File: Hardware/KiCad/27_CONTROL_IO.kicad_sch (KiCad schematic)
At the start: 0 parts

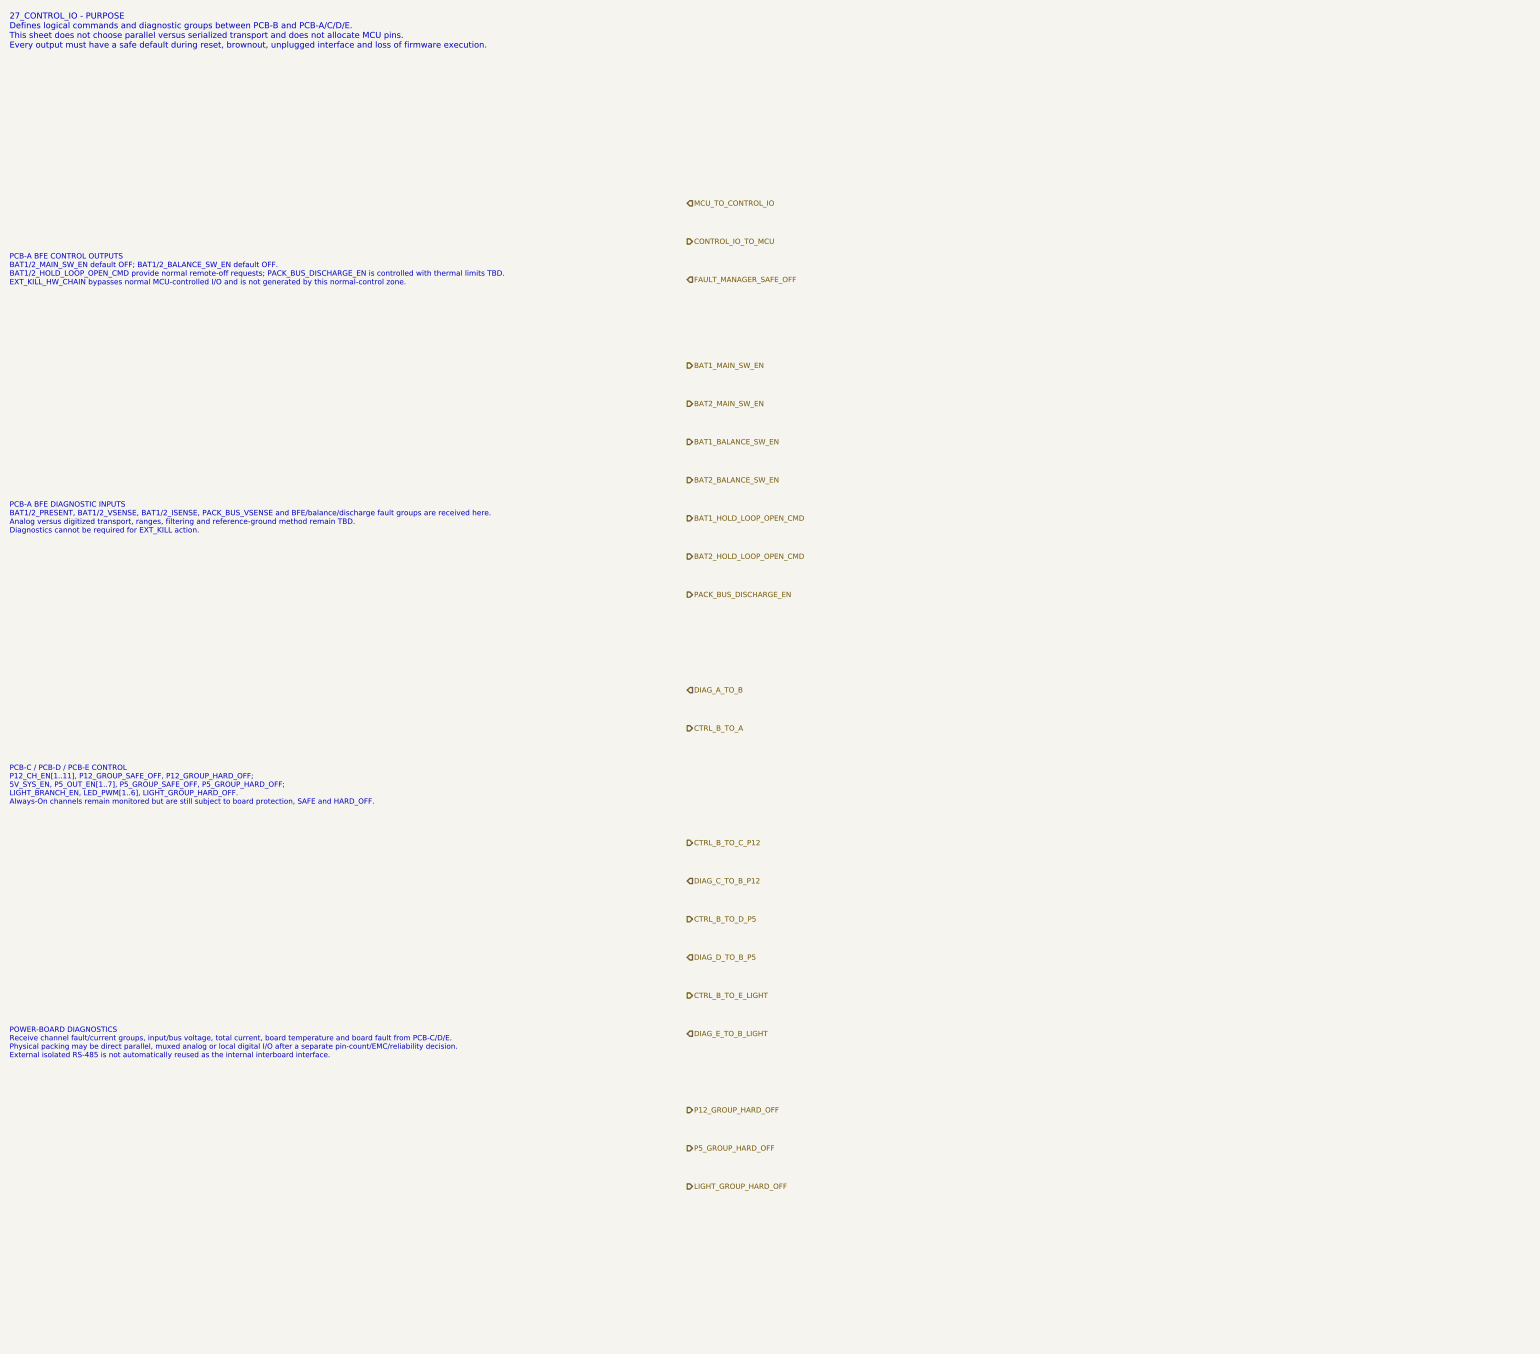
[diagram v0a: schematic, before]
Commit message: hardware: complete PCB-B control and diagnostic interfaces
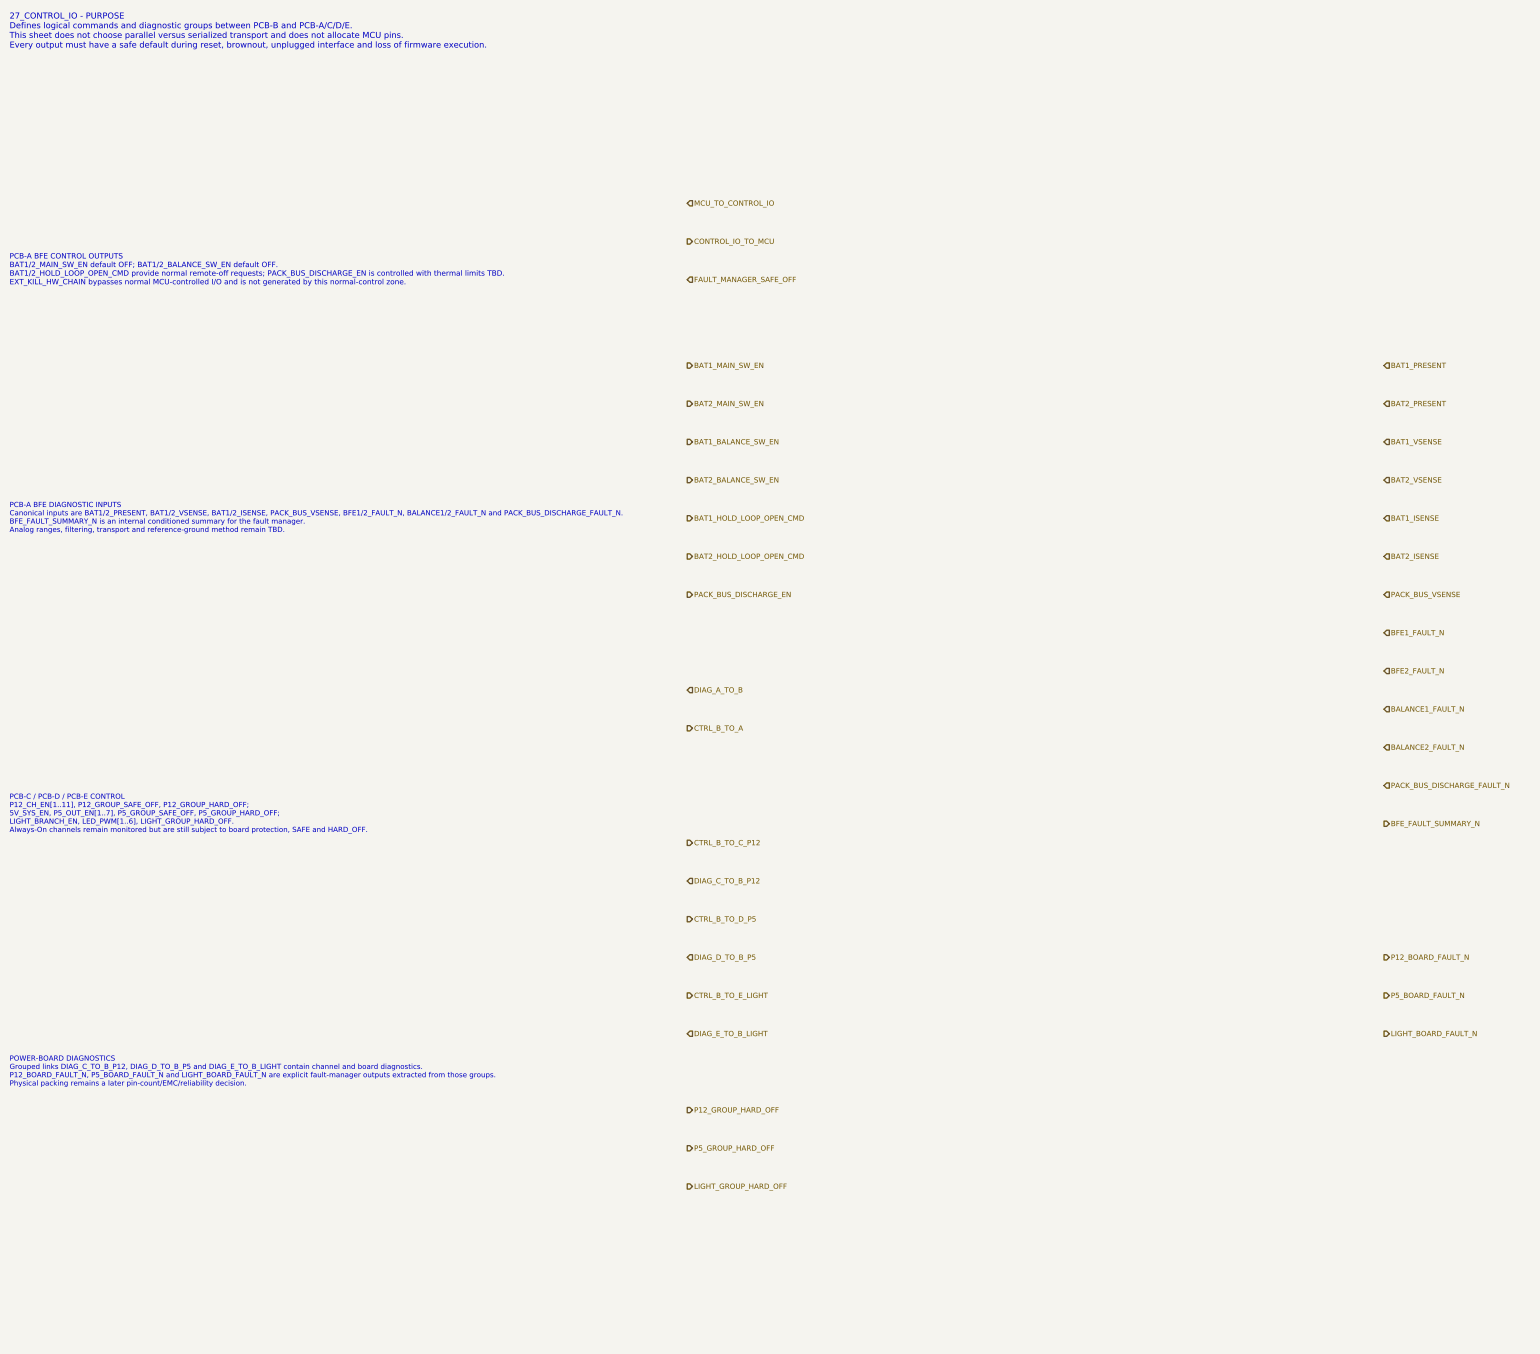
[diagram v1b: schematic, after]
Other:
- note added: "PCB-A BFE DIAGNOSTIC INPUTS Canonical inputs are BAT1/2_PRESENT, BAT1/2_VSENSE, BAT1/2_ISENSE, PACK_BUS_VSENSE, BFE1/2_FAULT_N, BALANCE1/2_FAULT_N and PACK_BUS_DISCHARGE_FAULT_N. BFE_FAULT_SUMMARY_N is an internal conditioned summary for the fault manager. Analog ranges, filtering, transport and reference-ground method remain TBD."
- note added: "POWER-BOARD DIAGNOSTICS Grouped links DIAG_C_TO_B_P12, DIAG_D_TO_B_P5 and DIAG_E_TO_B_LIGHT contain channel and board diagnostics. P12_BOARD_FAULT_N, P5_BOARD_FAULT_N and LIGHT_BOARD_FAULT_N are explicit fault-manager outputs extracted from those groups. Physical packing remains a later pin-count/EMC/reliability decision."
- note removed: "PCB-A BFE DIAGNOSTIC INPUTS BAT1/2_PRESENT, BAT1/2_VSENSE, BAT1/2_ISENSE, PACK_BUS_VSENSE and BFE/balance/discharge fault groups are received here. Analog versus digitized transport, ranges, filtering and reference-ground method remain TBD. Diagnostics cannot be required for EXT_KILL action."
- note removed: "POWER-BOARD DIAGNOSTICS Receive channel fault/current groups, input/bus voltage, total current, board temperature and board fault from PCB-C/D/E. Physical packing may be direct parallel, muxed analog or local digital I/O after a separate pin-count/EMC/reliability decision. External isolated RS-485 is not automatically reused as the internal interboard interface."
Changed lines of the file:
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@@
 		(title "27_CONTROL_IO - interboard control and diagnostics boundary")
 		(date "2026-07-15")
-		(rev "B0")
+		(rev "B1")
 		(company "Gonoboben/plataVM")
-		(comment 1 "Architecture Level A/B: BFE, POWER_12V, POWER_5V and LIGHT control/diagnostic groups")
+		(comment 1 "Interface consistency: canonical PCB-A diagnostics and board-fault summaries")
 		(comment 2 "No GPIO expander, ADC, mux, serializer, isolator, level shifter, connector or footprint selected")
 	)
@@
 		(uuid "ctrl-reserve-00000027-0000-4000-8000-000000000102")
 	)
-	(text "PCB-A BFE DIAGNOSTIC INPUTS\nBAT1/2_PRESENT, BAT1/2_VSENSE, BAT1/2_ISENSE, PACK_BUS_VSENSE and BFE/balance/discharge fault groups are received here.\nAnalog versus digitized transport, ranges, filtering and reference-ground method remain TBD.\nDiagnostics cannot be required for EXT_KILL action."
+	(text "PCB-A BFE DIAGNOSTIC INPUTS\nCanonical inputs are BAT1/2_PRESENT, BAT1/2_VSENSE, BAT1/2_ISENSE, PACK_BUS_VSENSE, BFE1/2_FAULT_N, BALANCE1/2_FAULT_N and PACK_BUS_DISCHARGE_FAULT_N.\nBFE_FAULT_SUMMARY_N is an internal conditioned summary for the fault manager.\nAnalog ranges, filtering, transport and reference-ground method remain TBD."
 		(exclude_from_sim no)
 		(at 12 114 0)
-		(effects (font (size 1.12 1.12)) (justify left))
+		(effects (font (size 1.08 1.08)) (justify left))
 		(uuid "ctrl-reserve-00000027-0000-4000-8000-000000000103")
 	)
 	(text "PCB-C / PCB-D / PCB-E CONTROL\nP12_CH_EN[1..11], P12_GROUP_SAFE_OFF, P12_GROUP_HARD_OFF;\n5V_SYS_EN, P5_OUT_EN[1..7], P5_GROUP_SAFE_OFF, P5_GROUP_HARD_OFF;\nLIGHT_BRANCH_EN, LED_PWM[1..6], LIGHT_GROUP_HARD_OFF.\nAlways-On channels remain monitored but are still subject to board protection, SAFE and HARD_OFF."
 		(exclude_from_sim no)
-		(at 12 170 0)
-		(effects (font (size 1.10 1.10)) (justify left))
+		(at 12 176 0)
+		(effects (font (size 1.08 1.08)) (justify left))
 		(uuid "ctrl-reserve-00000027-0000-4000-8000-000000000104")
 	)
-	(text "POWER-BOARD DIAGNOSTICS\nReceive channel fault/current groups, input/bus voltage, total current, board temperature and board fault from PCB-C/D/E.\nPhysical packing may be direct parallel, muxed analog or local digital I/O after a separate pin-count/EMC/reliability decision.\nExternal isolated RS-485 is not automatically reused as the internal interboard interface."
+	(text "POWER-BOARD DIAGNOSTICS\nGrouped links DIAG_C_TO_B_P12, DIAG_D_TO_B_P5 and DIAG_E_TO_B_LIGHT contain channel and board diagnostics.\nP12_BOARD_FAULT_N, P5_BOARD_FAULT_N and LIGHT_BOARD_FAULT_N are explicit fault-manager outputs extracted from those groups.\nPhysical packing remains a later pin-count/EMC/reliability decision."
 		(exclude_from_sim no)
-		(at 12 224 0)
-		(effects (font (size 1.10 1.10)) (justify left))
+		(at 12 230 0)
+		(effects (font (size 1.08 1.08)) (justify left))
 		(uuid "ctrl-reserve-00000027-0000-4000-8000-000000000105")
 	)
@@
 	(hierarchical_label "DIAG_A_TO_B" (shape input) (exclude_from_sim no) (at 154 150 0) (effects (font (size 1.1 1.1)) (justify left)) (uuid "ctrl-reserve-00000027-0000-4000-8000-000000000211"))
 	(hierarchical_label "CTRL_B_TO_A" (shape output) (exclude_from_sim no) (at 154 158 0) (effects (font (size 1.1 1.1)) (justify left)) (uuid "ctrl-reserve-00000027-0000-4000-8000-000000000212"))
+	(hierarchical_label "BAT1_PRESENT" (shape input) (exclude_from_sim no) (at 300 82 0) (effects (font (size 1.1 1.1)) (justify left)) (uuid "ctrl-reserve-00000027-0000-4000-8000-000000000222"))
+	(hierarchical_label "BAT2_PRESENT" (shape input) (exclude_from_sim no) (at 300 90 0) (effects (font (size 1.1 1.1)) (justify left)) (uuid "ctrl-reserve-00000027-0000-4000-8000-000000000223"))
+	(hierarchical_label "BAT1_VSENSE" (shape input) (exclude_from_sim no) (at 300 98 0) (effects (font (size 1.1 1.1)) (justify left)) (uuid "ctrl-reserve-00000027-0000-4000-8000-000000000224"))
+	(hierarchical_label "BAT2_VSENSE" (shape input) (exclude_from_sim no) (at 300 106 0) (effects (font (size 1.1 1.1)) (justify left)) (uuid "ctrl-reserve-00000027-0000-4000-8000-000000000225"))
+	(hierarchical_label "BAT1_ISENSE" (shape input) (exclude_from_sim no) (at 300 114 0) (effects (font (size 1.1 1.1)) (justify left)) (uuid "ctrl-reserve-00000027-0000-4000-8000-000000000226"))
+	(hierarchical_label "BAT2_ISENSE" (shape input) (exclude_from_sim no) (at 300 122 0) (effects (font (size 1.1 1.1)) (justify left)) (uuid "ctrl-reserve-00000027-0000-4000-8000-000000000227"))
+	(hierarchical_label "PACK_BUS_VSENSE" (shape input) (exclude_from_sim no) (at 300 130 0) (effects (font (size 1.1 1.1)) (justify left)) (uuid "ctrl-reserve-00000027-0000-4000-8000-000000000228"))
+	(hierarchical_label "BFE1_FAULT_N" (shape input) (exclude_from_sim no) (at 300 138 0) (effects (font (size 1.1 1.1)) (justify left)) (uuid "ctrl-reserve-00000027-0000-4000-8000-000000000229"))
+	(hierarchical_label "BFE2_FAULT_N" (shape input) (exclude_from_sim no) (at 300 146 0) (effects (font (size 1.1 1.1)) (justify left)) (uuid "ctrl-reserve-00000027-0000-4000-8000-000000000230"))
+	(hierarchical_label "BALANCE1_FAULT_N" (shape input) (exclude_from_sim no) (at 300 154 0) (effects (font (size 1.1 1.1)) (justify left)) (uuid "ctrl-reserve-00000027-0000-4000-8000-000000000231"))
+	(hierarchical_label "BALANCE2_FAULT_N" (shape input) (exclude_from_sim no) (at 300 162 0) (effects (font (size 1.1 1.1)) (justify left)) (uuid "ctrl-reserve-00000027-0000-4000-8000-000000000232"))
+	(hierarchical_label "PACK_BUS_DISCHARGE_FAULT_N" (shape input) (exclude_from_sim no) (at 300 170 0) (effects (font (size 1.1 1.1)) (justify left)) (uuid "ctrl-reserve-00000027-0000-4000-8000-000000000233"))
+	(hierarchical_label "BFE_FAULT_SUMMARY_N" (shape output) (exclude_from_sim no) (at 300 178 0) (effects (font (size 1.1 1.1)) (justify left)) (uuid "ctrl-reserve-00000027-0000-4000-8000-000000000234"))
 	(hierarchical_label "CTRL_B_TO_C_P12" (shape output) (exclude_from_sim no) (at 154 182 0) (effects (font (size 1.1 1.1)) (justify left)) (uuid "ctrl-reserve-00000027-0000-4000-8000-000000000213"))
 	(hierarchical_label "DIAG_C_TO_B_P12" (shape input) (exclude_from_sim no) (at 154 190 0) (effects (font (size 1.1 1.1)) (justify left)) (uuid "ctrl-reserve-00000027-0000-4000-8000-000000000214"))
@@
 	(hierarchical_label "P5_GROUP_HARD_OFF" (shape output) (exclude_from_sim no) (at 154 246 0) (effects (font (size 1.1 1.1)) (justify left)) (uuid "ctrl-reserve-00000027-0000-4000-8000-000000000220"))
 	(hierarchical_label "LIGHT_GROUP_HARD_OFF" (shape output) (exclude_from_sim no) (at 154 254 0) (effects (font (size 1.1 1.1)) (justify left)) (uuid "ctrl-reserve-00000027-0000-4000-8000-000000000221"))
+	(hierarchical_label "P12_BOARD_FAULT_N" (shape output) (exclude_from_sim no) (at 300 206 0) (effects (font (size 1.1 1.1)) (justify left)) (uuid "ctrl-reserve-00000027-0000-4000-8000-000000000235"))
+	(hierarchical_label "P5_BOARD_FAULT_N" (shape output) (exclude_from_sim no) (at 300 214 0) (effects (font (size 1.1 1.1)) (justify left)) (uuid "ctrl-reserve-00000027-0000-4000-8000-000000000236"))
+	(hierarchical_label "LIGHT_BOARD_FAULT_N" (shape output) (exclude_from_sim no) (at 300 222 0) (effects (font (size 1.1 1.1)) (justify left)) (uuid "ctrl-reserve-00000027-0000-4000-8000-000000000237"))
 )
